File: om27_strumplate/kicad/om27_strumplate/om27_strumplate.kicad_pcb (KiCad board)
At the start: 2 copper layers, 112.1 x 159.1 mm, 0 parts

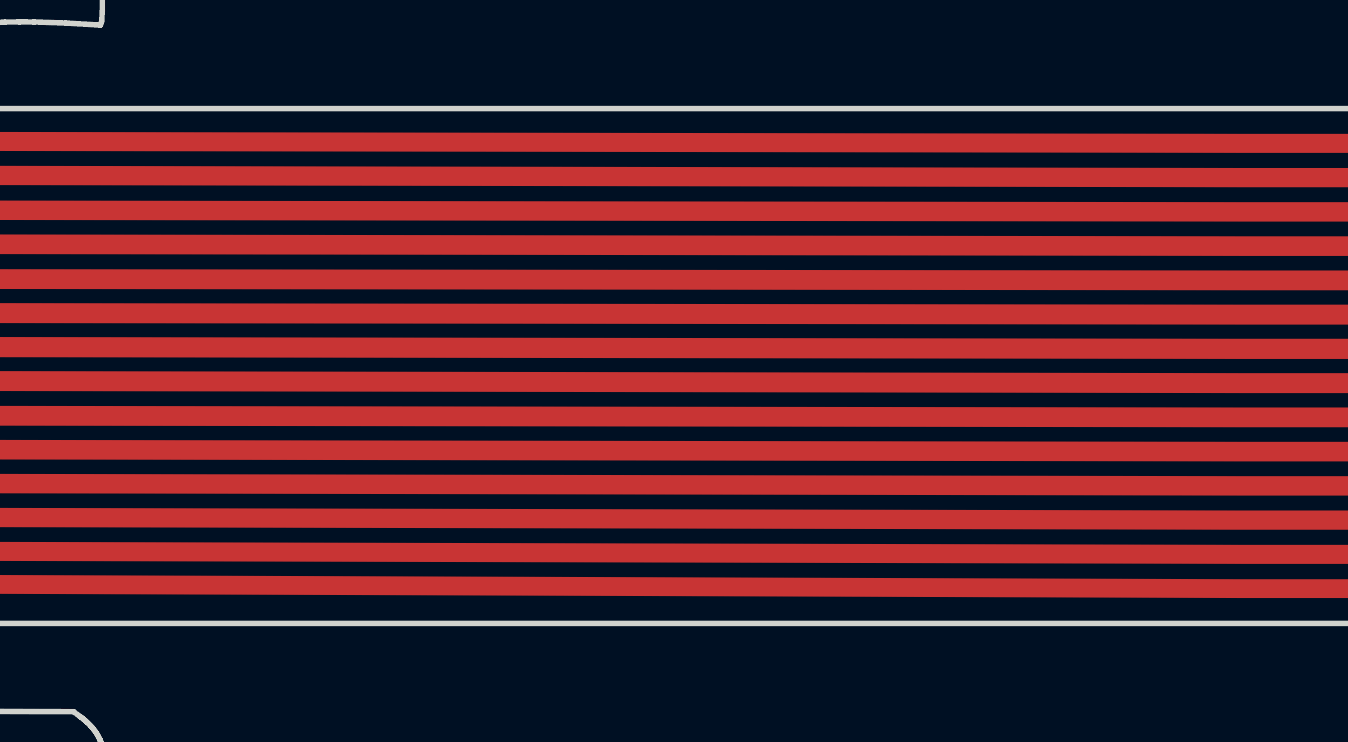
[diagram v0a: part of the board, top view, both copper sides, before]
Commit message: Add Key & Cable Co. branding to both flex tails
White silkscreen on the ribbon tail of the OM-84 and OM-27 flex PCBs:
the piano-key mark (10 mm, white key outlined, black key and plug
filled, cable as a 0.25 mm stroke), "Key & Cable Co." and
"keyandcable.com" in stroke text, and a QR code for
https://keyandcable.com. The QR is version 3 at ECC level H; the ink
prints the light modules and a 3-module quiet zone so the amber
coverlay forms the dark modules. OM-84 uses 0.45 mm modules, the
narrower OM-27 tail uses 0.42 mm. Everything sits over the traces,
clear of the contacts, mask openings and gold-finger stiffeners.

The artwork lives in lib/keyandcable_branding.pretty as reusable
footprints, with a project fp-lib-table in each KiCad folder.
F_Silkscreen gerbers re-plotted with the stored board plot settings
and the production zips updated.

Co-Authored-By: Claude Fable 5.1 <noreply@anthropic.com>
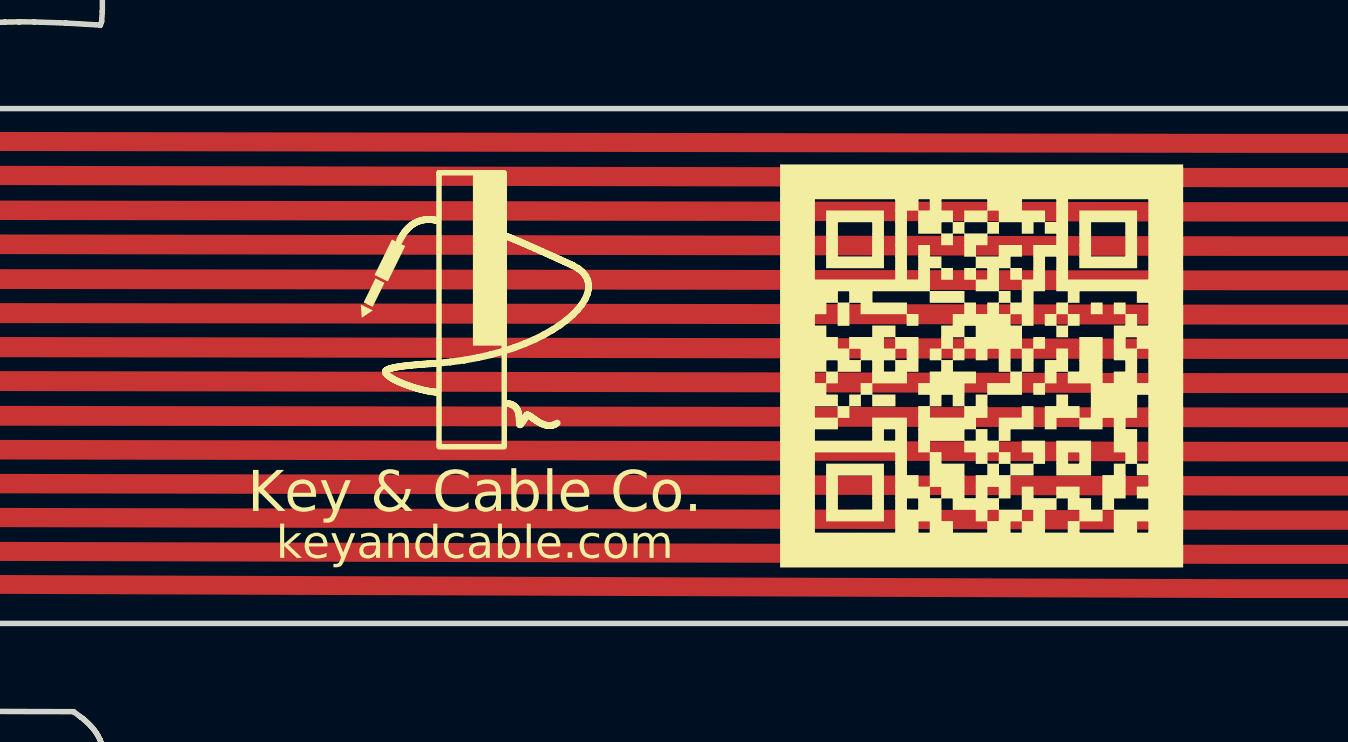
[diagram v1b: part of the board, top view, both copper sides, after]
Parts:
- added REF**: KeyAndCable_Logo, keyandcable_branding:KeyAndCable_Logo, F.Cu at (157.0, 79.2)
- added REF**: KeyAndCable_QR_42, keyandcable_branding:KeyAndCable_QR_42, F.Cu at (175.5, 79.2)

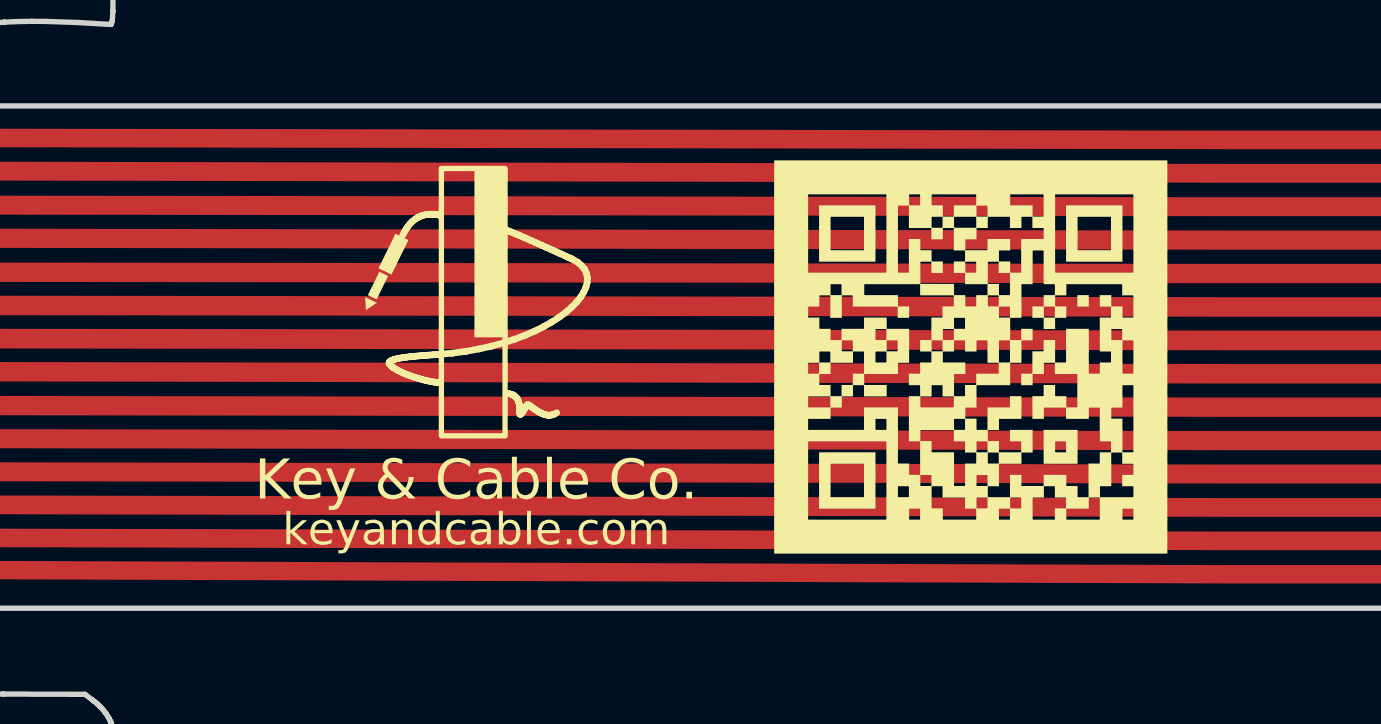
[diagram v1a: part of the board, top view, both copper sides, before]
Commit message: Label both flex tails with model and version V1.1
Each tail now carries its model in bold 2 mm silkscreen ("OM-84" /
"OM-27") with the version under it. The version is printed from the
board's title-block revision via ${REVISION}, so it is bumped in
Board Setup > Title Block and also lands in the Gerber X2 headers.
Both boards are set to 1.1: V1.0 was the first fab run, V1.1 adds the
1.25 mm finger pitch fix and the Key & Cable branding.

On the OM-84 the labels sit horizontally between the logo and the QR.
The OM-27 tail has about 40 mm between the bend and the stiffener, so
its labels are rotated 90 degrees into a column, and the logo and QR
are re-spaced to keep at least 1.3 mm between elements and 1.3 mm
from the stiffener. The company name in the logo lockup drops from
1.5 mm to 1.3 mm text to make room.

F_Silkscreen gerbers re-plotted and the production zips updated.

Co-Authored-By: Claude Opus 5.5 <noreply@anthropic.com>
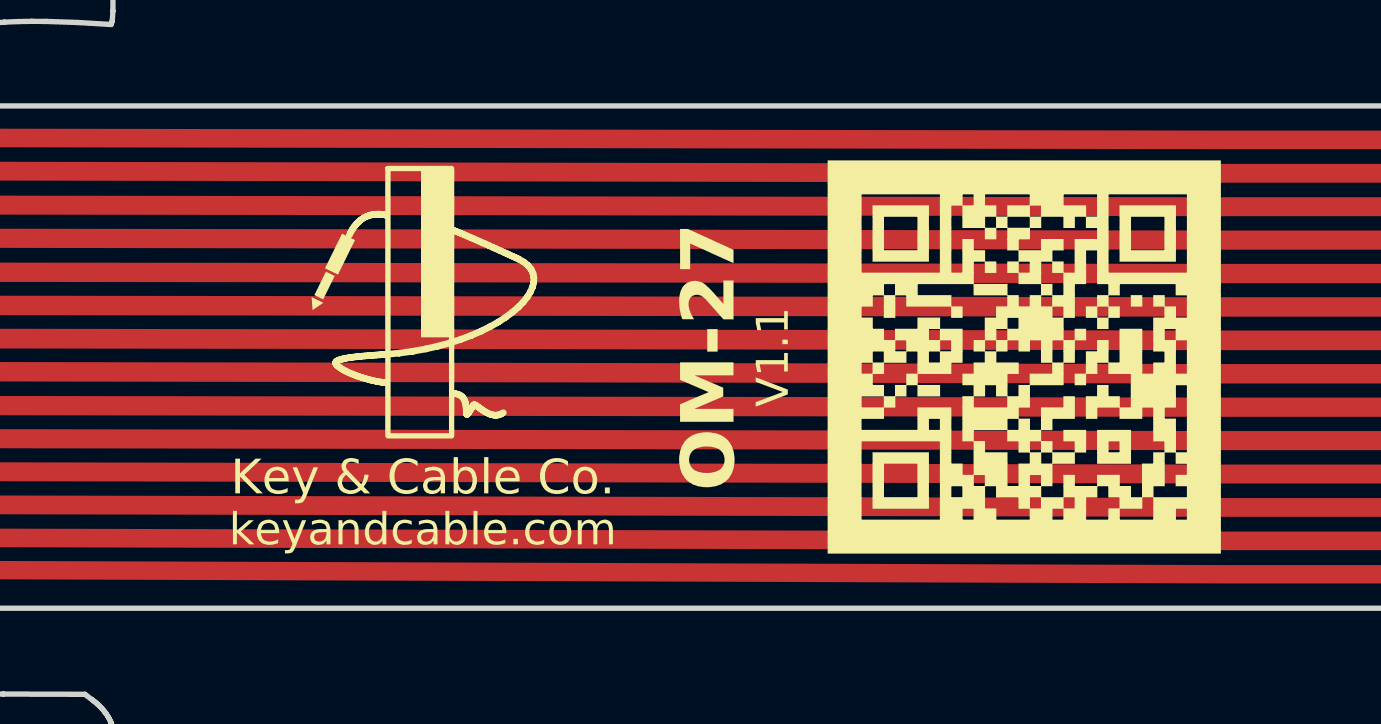
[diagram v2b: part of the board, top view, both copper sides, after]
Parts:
- moved REF** 2.00 mm to (155.0, 79.2)
- moved REF** 2.00 mm to (177.5, 79.2)
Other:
- board text added: "OM-27"
- board text added: "V${REVISION}"
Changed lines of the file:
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@@
 	)
 	(paper "A4")
+	(title_block
+		(title "OM-27 Strumplate Flex PCB")
+		(date "2026-10-08")
+		(rev "1.1")
+		(company "Key & Cable Co.")
+	)
 	(layers
 		(0 "F.Cu" signal)
@@
 	(footprint "keyandcable_branding:KeyAndCable_Logo"
 		(layer "F.Cu")
-		(at 157 79.165)
+		(at 155.0 79.165)
 		(descr "Key and Cable Co. logo lockup for white silkscreen: piano-key mark, company name and web address")
 		(tags "logo silkscreen keyandcable")
@@
 		)
 		(fp_text user "Key & Cable Co."
-			(at 0 4.6 0)
+			(at 0 4.5 0)
 			(layer "F.SilkS")
 			(effects
 				(font
-					(size 1.5 1.5)
-					(thickness 0.18)
+					(size 1.3 1.3)
+					(thickness 0.16)
 				)
 			)
@@
 	(footprint "keyandcable_branding:KeyAndCable_QR_42"
 		(layer "F.Cu")
-		(at 175.5 79.165)
+		(at 177.5 79.165)
 		(descr "QR code for https://keyandcable.com, white silkscreen prints the light modules and quiet zone, ECC level H")
 		(tags "qr silkscreen keyandcable")
@@
 		(embedded_fonts no)
 	)
+	(gr_text "OM-27"
+		(at 165.7 79.165 90)
+		(layer "F.SilkS")
+		(effects
+			(font
+				(size 2 2)
+				(thickness 0.3)
+				(bold yes)
+			)
+		)
+	)
+	(gr_text "V${REVISION}"
+		(at 168.1 79.165 90)
+		(layer "F.SilkS")
+		(effects
+			(font
+				(size 1.2 1.2)
+				(thickness 0.18)
+			)
+		)
+	)
 	(gr_poly
